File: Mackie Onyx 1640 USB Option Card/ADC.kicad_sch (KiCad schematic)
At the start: 1 part, among them U2 TLV320ADC5140IRTWR

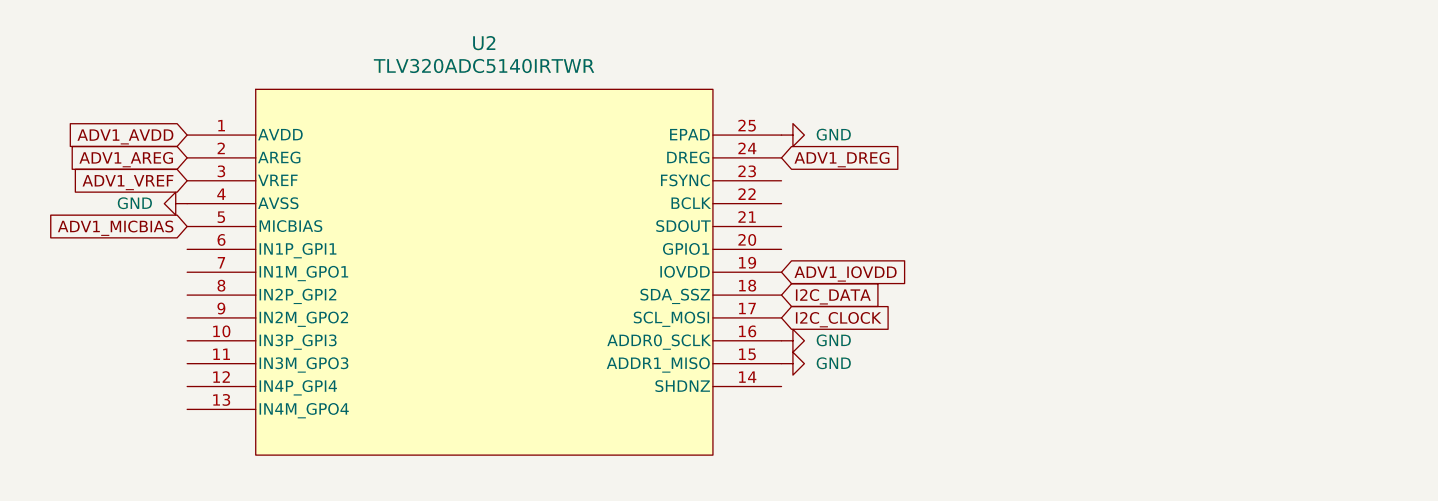
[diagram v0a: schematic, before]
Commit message: Added Balancing Circuit ADC input is balanced, card connector isnt schematic following the one from original firewire card since ADC input voltage ratings are very close quad-op-amp-ic is placeholder with standard footprint, a higher quality one may be used on BOM did a bit of more or less rough PCB layouting
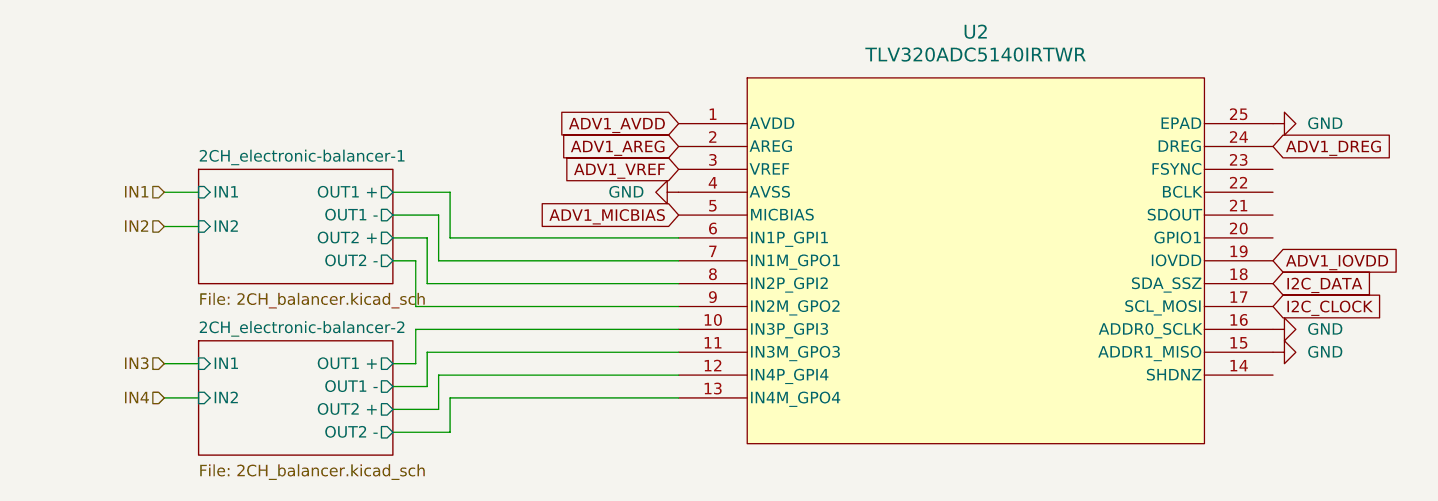
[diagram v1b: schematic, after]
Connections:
- net 2CH_electronic-balancer-2/OUT1 +: now reaches U2.10 (IN3P_GPI3)
- net 2CH_electronic-balancer-2/OUT1 -: now reaches U2.11 (IN3M_GPO3)
- net 2CH_electronic-balancer-2/OUT2 +: now reaches U2.12 (IN4P_GPI4)
- net 2CH_electronic-balancer-2/OUT2 -: now reaches U2.13 (IN4M_GPO4)
- net 2CH_electronic-balancer-1/OUT1 +: now reaches U2.6 (IN1P_GPI1)
- net 2CH_electronic-balancer-1/OUT1 -: now reaches U2.7 (IN1M_GPO1)
- net 2CH_electronic-balancer-1/OUT2 +: now reaches U2.8 (IN2P_GPI2)
- net 2CH_electronic-balancer-1/OUT2 -: now reaches U2.9 (IN2M_GPO2)
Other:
- added sheet 2CH_electronic-balancer-1 (2CH_balancer.kicad_sch)
- added sheet 2CH_electronic-balancer-2 (2CH_balancer.kicad_sch)
- moved on the sheet: U2
